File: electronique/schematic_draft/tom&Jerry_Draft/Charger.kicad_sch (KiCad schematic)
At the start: 20 parts, among them SW5 Switch, U1 MP1475DJ-LF-P

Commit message: STM32 KiCAD V2 - 18.09.2024
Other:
- note added: "3A"
- note removed: "Linear regulator"
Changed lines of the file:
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@@
+	)
+	(junction
+		(at 29.21 41.91)
+		(diameter 0)
+		(color 0 0 0 0)
 	)
 	(junction
@@
 	)
 	(junction
+		(at 58.42 74.93)
+		(diameter 0)
+		(color 0 0 0 0)
+	)
+	(junction
 		(at 44.45 54.61)
 		(diameter 0)
@@
 	)
 	(junction
+		(at 120.65 59.69)
+		(diameter 0)
+		(color 0 0 0 0)
+	)
+	(junction
 		(at 91.44 59.69)
 		(diameter 0)
@@
 	(wire
 		(pts
-			(xy 29.21 39.37) (xy 29.21 54.61)
+			(xy 29.21 39.37) (xy 29.21 41.91)
 		)
 		(stroke
@@
 		(pts
 			(xy 106.68 71.12) (xy 106.68 64.77)
+		)
+		(stroke
+			(width 0)
+			(type default)
+		)
+	)
+	(wire
+		(pts
+			(xy 29.21 41.91) (xy 29.21 54.61)
 		)
 		(stroke
@@
 		)
 	)
-	(text "Linear regulator\n\n\n"
-		(exclude_from_sim no)
-		(at 173.99 36.83 0)
-		(effects
-			(font
-				(size 4 4)
-				(bold yes)
-				(color 255 0 48 1)
-			)
-			(justify left bottom)
-		)
-	)
 	(text "recommanded components"
 		(exclude_from_sim no)
@@
 		)
 	)
-	(label "3A"
-		(at 114.3 59.69 0)
-		(fields_autoplaced yes)
+	(text "3A\n"
+		(exclude_from_sim no)
+		(at 116.332 59.182 0)
 		(effects
 			(font
 				(size 1.27 1.27)
 			)
-			(justify left bottom)
 		)
 	)
@@
 	)
 	(symbol
+		(lib_id "power:PWR_FLAG")
+		(at 29.21 41.91 90)
+		(unit 1)
+		(exclude_from_sim no)
+		(in_bom yes)
+		(on_board yes)
+		(dnp no)
+		(fields_autoplaced yes)
+		(property "Reference" "#FLG0201"
+			(at 27.305 41.91 0)
+			(effects
+				(font
+					(size 1.27 1.27)
+				)
+				(hide yes)
+			)
+		)
+		(property "Value" "PWR_FLAG"
+			(at 25.4 41.9099 90)
+			(effects
+				(font
+					(size 1.27 1.27)
+				)
+				(justify left)
+			)
+		)
+		(property "Footprint" ""
+			(at 29.21 41.91 0)
+			(effects
+				(font
+					(size 1.27 1.27)
+				)
+				(hide yes)
+			)
+		)
+		(property "Datasheet" "~"
+			(at 29.21 41.91 0)
+			(effects
+				(font
+					(size 1.27 1.27)
+				)
+				(hide yes)
+			)
+		)
+		(property "Description" "Special symbol for telling ERC where power comes from"
+			(at 29.21 41.91 0)
+			(effects
+				(font
+					(size 1.27 1.27)
+				)
+				(hide yes)
+			)
+		)
+		(pin "1"
+		)
+		(instances
+			(project ""
+				(path "/d6e3fbeb-d028-494d-83bf-2e4a8b12578d/8ac3fdfa-c0da-499a-9332-dcbe4f0edf5d"
+					(reference "#FLG0201")
+					(unit 1)
+				)
+			)
+		)
+	)
+	(symbol
 		(lib_id "Device:R_Small")
 		(at 82.55 71.12 90)
@@
 	)
 	(symbol
+		(lib_id "power:PWR_FLAG")
+		(at 120.65 59.69 270)
+		(unit 1)
+		(exclude_from_sim no)
+		(in_bom yes)
+		(on_board yes)
+		(dnp no)
+		(fields_autoplaced yes)
+		(property "Reference" "#FLG0202"
+			(at 122.555 59.69 0)
+			(effects
+				(font
+					(size 1.27 1.27)
+				)
+				(hide yes)
+			)
+		)
+		(property "Value" "PWR_FLAG"
+			(at 124.46 59.6899 90)
+			(effects
+				(font
+					(size 1.27 1.27)
+				)
+				(justify left)
+			)
+		)
+		(property "Footprint" ""
+			(at 120.65 59.69 0)
+			(effects
+				(font
+					(size 1.27 1.27)
+				)
+				(hide yes)
+			)
+		)
+		(property "Datasheet" "~"
+			(at 120.65 59.69 0)
+			(effects
+				(font
+					(size 1.27 1.27)
+				)
+				(hide yes)
+			)
+		)
+		(property "Description" "Special symbol for telling ERC where power comes from"
+			(at 120.65 59.69 0)
+			(effects
+				(font
+					(size 1.27 1.27)
+				)
+				(hide yes)
+			)
+		)
+		(pin "1"
+		)
+		(instances
+			(project "tom&Jerry_Draft"
+				(path "/d6e3fbeb-d028-494d-83bf-2e4a8b12578d/8ac3fdfa-c0da-499a-9332-dcbe4f0edf5d"
+					(reference "#FLG0202")
+					(unit 1)
+				)
+			)
+		)
+	)
+	(symbol
 		(lib_id "power:GND")
 		(at 95.25 52.07 180)
@@
 					(unit 1)
 				)
+			)
+		)
+	)
+	(symbol
+		(lib_id "power:PWR_FLAG")
+		(at 58.42 74.93 90)
+		(unit 1)
+		(exclude_from_sim no)
+		(in_bom yes)
+		(on_board yes)
+		(dnp no)
+		(fields_autoplaced yes)
+		(property "Reference" "#FLG0203"
+			(at 56.515 74.93 0)
+			(effects
+				(font
+					(size 1.27 1.27)
+				)
+				(hide yes)
+			)
+		)
+		(property "Value" "PWR_FLAG"
+			(at 54.61 74.9299 90)
+			(effects
+				(font
+					(size 1.27 1.27)
+				)
+				(justify left)
+			)
+		)
+		(property "Footprint" ""
+			(at 58.42 74.93 0)
+			(effects
+				(font
+					(size 1.27 1.27)
+				)
+				(hide yes)
+			)
+		)
+		(property "Datasheet" "~"
+			(at 58.42 74.93 0)
+			(effects
+				(font
+					(size 1.27 1.27)
+				)
+				(hide yes)
+			)
+		)
+		(property "Description" "Special symbol for telling ERC where power comes from"
+			(at 58.42 74.93 0)
+			(effects
+				(font
+					(size 1.27 1.27)
+				)
+				(hide yes)
+			)
+		)
+		(pin "1"
+		)
+		(instances
+			(project "tom&Jerry_Draft"
+				(path "/d6e3fbeb-d028-494d-83bf-2e4a8b12578d/8ac3fdfa-c0da-499a-9332-dcbe4f0edf5d"
+					(reference "#FLG0203")
+					(unit 1)
+				)

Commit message: KiCAD V3 - 18.09.2024
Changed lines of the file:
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@@
+	(wire
+		(pts
+			(xy 175.26 87.63) (xy 175.26 90.17)
+		)
+		(stroke
+			(width 0)
+			(type default)
+		)
+	)
 	(wire
 		(pts
@@
 		)
 	)
+	(hierarchical_label "CC2"
+		(shape input)
+		(at 175.26 90.17 0)
+		(fields_autoplaced yes)
+		(effects
+			(font
+				(size 1.27 1.27)
+			)
+			(justify left)
+		)
+	)
+	(hierarchical_label "CC1"
+		(shape input)
+		(at 175.26 87.63 0)
+		(fields_autoplaced yes)
+		(effects
+			(font
+				(size 1.27 1.27)
+			)
+			(justify left)
+		)
+	)

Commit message: STM32 KiCAD V5 - 20.09.2024
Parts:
- removed Alim_batterie1, Alim_charger1: Conn_01x02, Connector_JST:JST_XH_S2B-XH-A-1_1x02_P2.50mm_Horizontal, symbol Connector_Generic:Conn_01x02
- removed C10, C11, C9: 0.1uF, Capacitor_SMD:C_0603_1608Metric_Pad1.08x0.95mm_HandSolder, symbol Device:C_Small
- removed C12: 15pF, Capacitor_SMD:C_0603_1608Metric_Pad1.08x0.95mm_HandSolder, symbol Device:C_Small
- removed C13, C14, C8: 22uF, Capacitor_SMD:C_0603_1608Metric_Pad1.08x0.95mm_HandSolder, symbol Device:C_Small
- removed D7: 1.5KExxA, Library:SODFL3718X108N, symbol Diode:1.5KExxA
- removed F1: Polyfuse, Fuse:Fuse_1206_3216Metric, symbol Device:Polyfuse
- removed L2: 4.7uH, Library:INDPM4141X210N, symbol Device:L_Small
- removed R10: 20, Resistor_SMD:R_0805_2012Metric_Pad1.20x1.40mm_HandSolder, symbol Device:R_Small
- removed R11: 16k, Resistor_SMD:R_0603_1608Metric_Pad0.98x0.95mm_HandSolder, symbol Device:R_Small
- removed R12: 7.36k, Resistor_SMD:R_0603_1608Metric_Pad0.98x0.95mm_HandSolder, symbol Device:R_Small
- removed R13: 40.2k, Resistor_SMD:R_0603_1608Metric_Pad0.98x0.95mm_HandSolder, symbol Device:R_Small
- removed R8, R9: 100k, Resistor_SMD:R_0603_1608Metric_Pad0.98x0.95mm_HandSolder, symbol Device:R_Small
- removed SW5: Switch, Library:Switch-3, symbol Switch:SW_SPDT
- removed U1: MP1475DJ-LF-P, Library:SOT65P280X100-8N, symbol Ludzlib:MP1475
- added C201, C206, C207: 22uF, Capacitor_SMD:C_0603_1608Metric_Pad1.08x0.95mm_HandSolder, symbol Device:C_Small
- added C202, C203, C204: 0.1uF, Capacitor_SMD:C_0603_1608Metric_Pad1.08x0.95mm_HandSolder, symbol Device:C_Small
- added C205: 15pF, Capacitor_SMD:C_0603_1608Metric_Pad1.08x0.95mm_HandSolder, symbol Device:C_Small
- added C208, C209: 1uF, symbol Device:C
- added C210, C212: 10nF, symbol Device:C
- added C211: 100nF, symbol Device:C
- added C213: 1mF, symbol Device:C
- added D201: LED, symbol Device:LED
- added D202, D203: D, symbol Device:D
- added J201: USB_C_Receptacle_USB2.0_16P, symbol Connector:USB_C_Receptacle_USB2.0_16P
- added J202, J203: Conn_01x02, symbol Connector_Generic:Conn_01x02
- added JP201, JP202, JP203, JP204: SolderJumper_2_Open, symbol Jumper:SolderJumper_2_Open
- added L201: 4.7uH, Library:INDPM4141X210N, symbol Device:L_Small
- added PS201: BU33SD5WG-TR, BU33SD5WG-TR:SOT95P280X125-5N, symbol BU33SD5WG-TR:BU33SD5WG-TR
- added R201, R202: 100k, Resistor_SMD:R_0603_1608Metric_Pad0.98x0.95mm_HandSolder, symbol Device:R_Small
- added R203: 20, Resistor_SMD:R_0805_2012Metric_Pad1.20x1.40mm_HandSolder, symbol Device:R_Small
- added R204: 16k, Resistor_SMD:R_0603_1608Metric_Pad0.98x0.95mm_HandSolder, symbol Device:R_Small
- added R205: 7.36k, Resistor_SMD:R_0603_1608Metric_Pad0.98x0.95mm_HandSolder, symbol Device:R_Small
- added R206: 40.2k, Resistor_SMD:R_0603_1608Metric_Pad0.98x0.95mm_HandSolder, symbol Device:R_Small
- added R207: 3.6k, symbol Device:R
- added R208, R209: 27K, symbol Device:R
- added R210: 10k, symbol Device:R
- added R211: 15k, symbol Device:R
- added R212: 100m, symbol Device:R
- added U201: MP1475DJ-LF-P, Library:SOT65P280X100-8N, symbol Ludzlib:MP1475
- added U202: BQ25172DSGR, BQ25172DSGR:IC_BQ25172DSGR, symbol BQ25172:BQ25172DSGR
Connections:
- net +5V: now also C205.2, C206.1, C207.1, C208.1, L201.2, PS201.1 (VIN), PS201.3 (STBY), R206.2
- net +BATT: now also C201.1, C203.1, C211.1, C212.1, D202.1 (K), JP202.2 (B), R202.2, R212.1, U201.2 (IN)
- net CC1: now also J201.A5 (CC1)
- net GND: now also C201.2, C202.1, C203.2, C206.2, C207.2, C208.2, C209.2, C210.2, C211.2, C212.2, C213.2, J201.A1 (GND), J201.A12 (GND), J201.B1 (GND), J201.B12 (GND), J201.S1 (SHIELD), J202.1 (Pin_1), J203.1 (Pin_1), PS201.2 (GND), R205.1, R207.2, R208.2, R209.2, R210.2, R211.2, U201.4 (GND), U202.4 (GND), U202.9 (EXP)
- new net: C213.1, R212.2
- new net: C204.1, L201.1, U201.3 (SW)
- new net: C205.1, R204.2, R205.2, R206.1
- new net: R208.1, U202.6 (TMR)
- new net: JP204.1 (A), U202.1 (IN)
- new net: R209.1, U202.2 (ISET)
- new net: R210.1, U202.3 (TS)
- new net: D201.1 (K), U202.5 (STAT)
- new net: R207.1, U202.7 (VSET)
- new net: C210.1, D203.1 (K), R211.1
- new net: R201.1, U201.1 (PG)
- new net: C202.2, R201.2, U201.7 (VCC)
- new net: R204.1, U201.8 (FB)
- new net: R203.1, U201.5 (BST)
- new net: C204.2, R203.2
- new net: D202.2 (A), D203.2 (A), JP201.2 (B)
- new net: R202.1, U201.6 (EN/SYNC)
- new net +3.3V: C209.1, D201.2 (A), PS201.5 (VOUT)
- new net Batt_CHG: J201.A4 (VBUS), J201.A9 (VBUS), J201.B4 (VBUS), J201.B9 (VBUS), J202.2 (Pin_2), JP201.1 (A), JP204.2 (B)
- new net Batt_cell: J203.2 (Pin_2), JP203.1 (A), U202.8 (OUT)
- new net CC2: J201.B5 (CC2)
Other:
- note added: "Linear regulator"
- note added: "Valeure minimale des condo (cf doc)"
- note removed: "3A"
- note removed: "Accepted current 1.5A Max current 3A ->5s"
- note removed: "Enable alway one"
- note removed: "recommanded components"

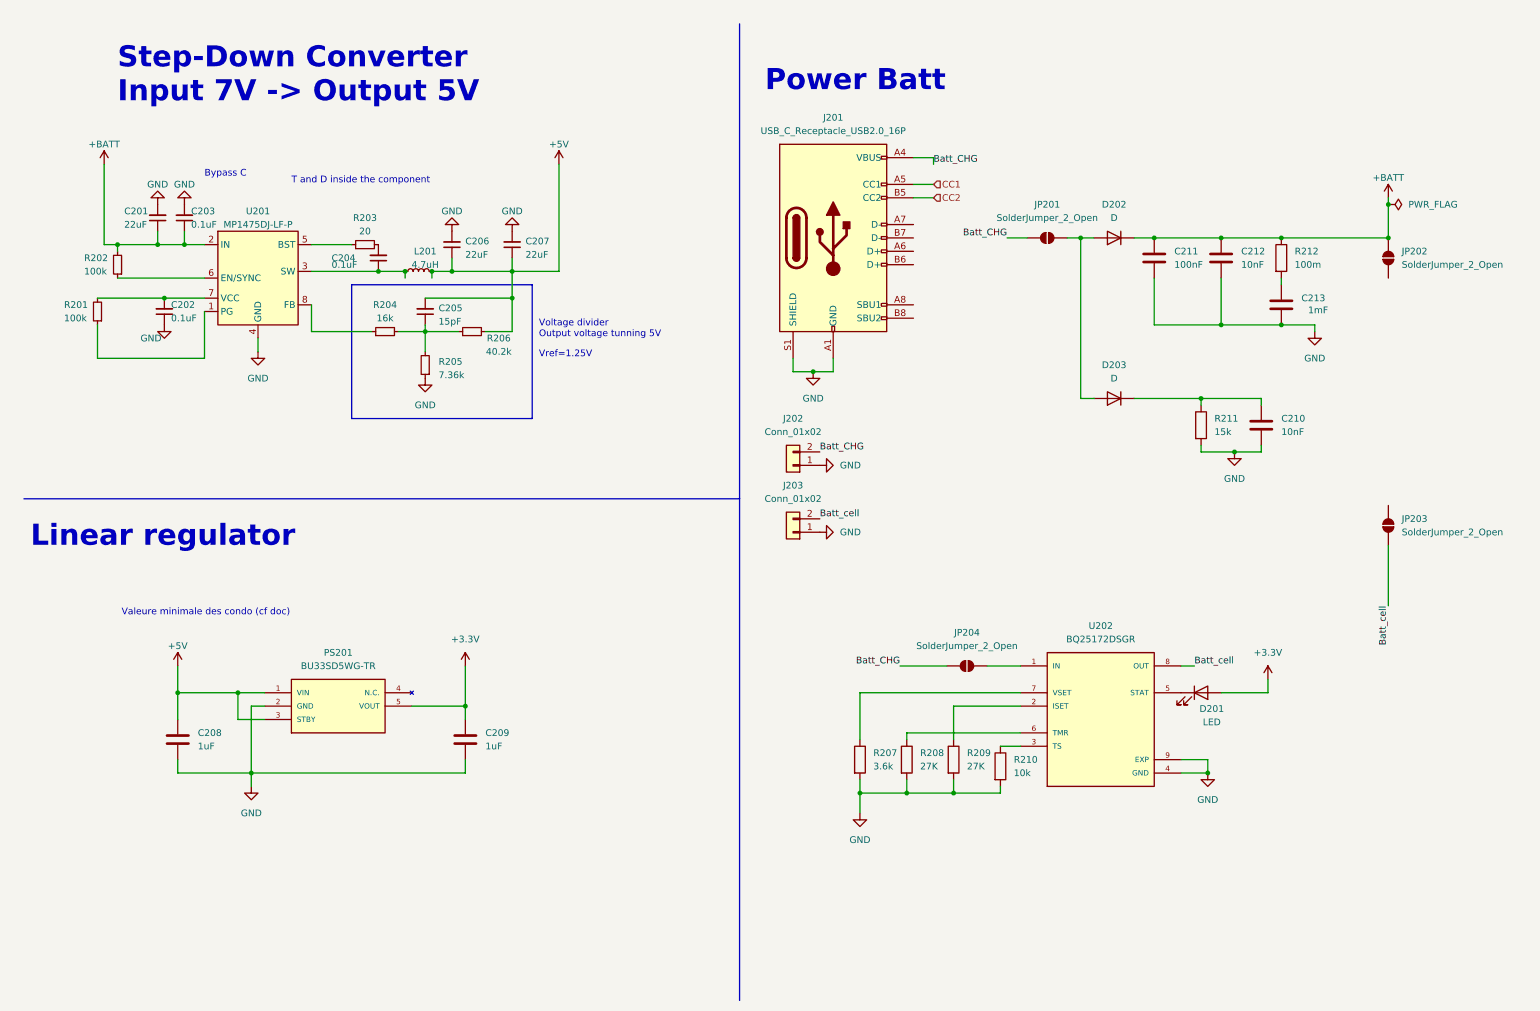
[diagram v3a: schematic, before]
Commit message: STM32 KiCAD V5 - 25.09.2024 - Ajout connecteurs TOF, ...
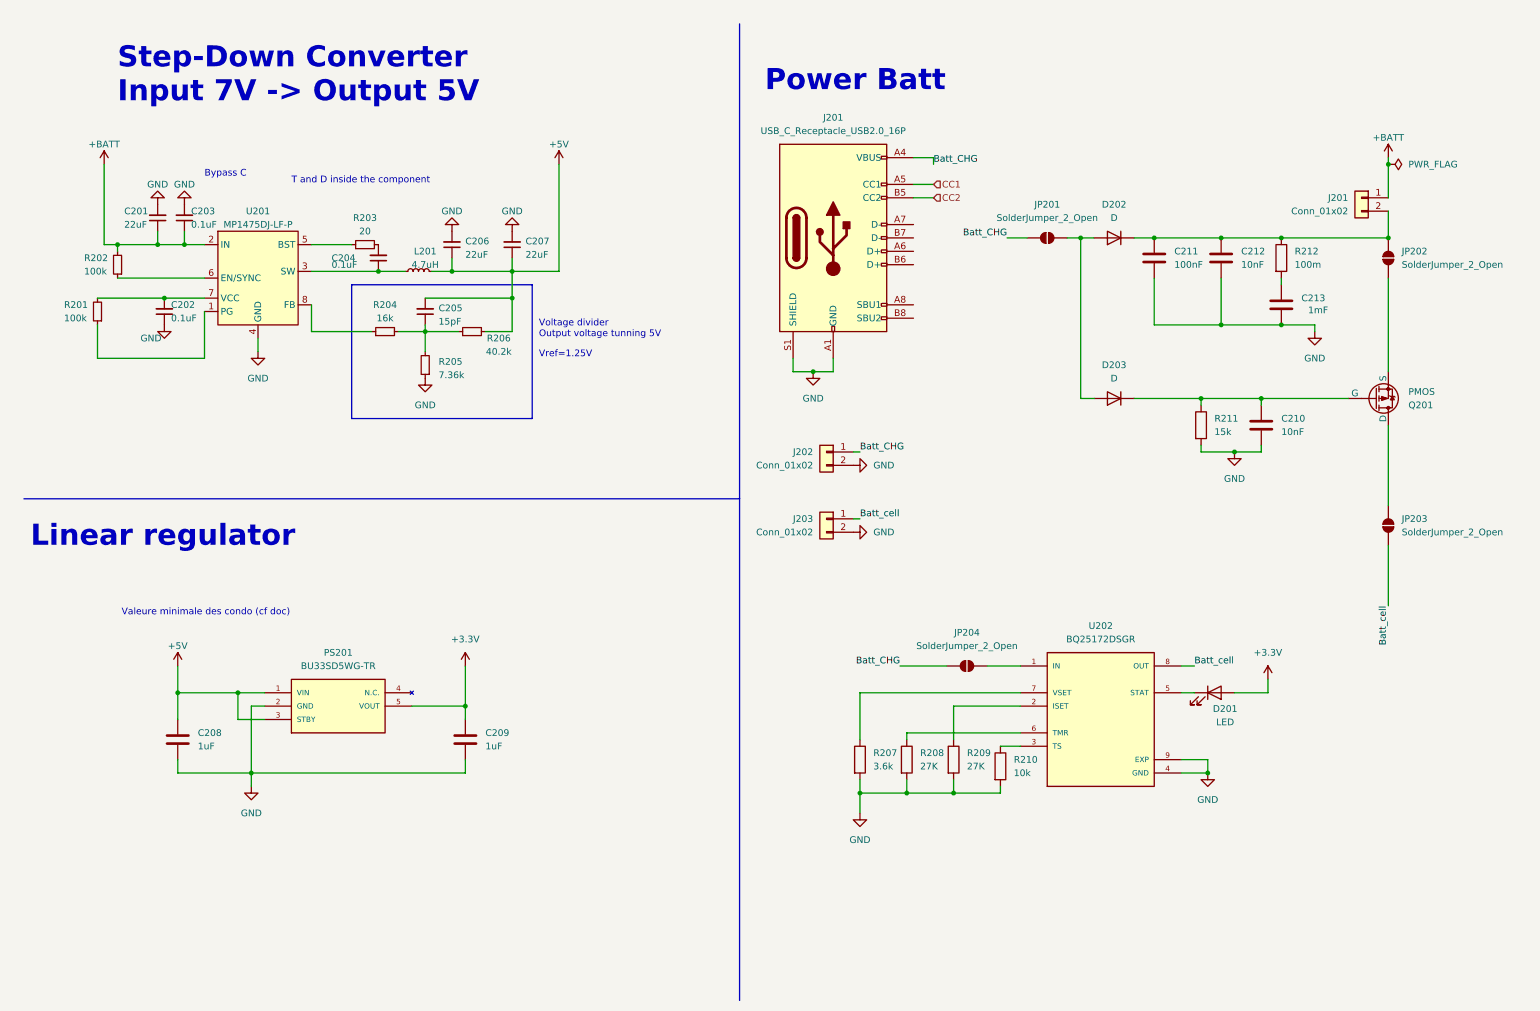
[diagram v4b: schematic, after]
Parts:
- added J201: Conn_01x02, symbol Connector_Generic:Conn_01x02
- added Q201: PMOS, symbol Simulation_SPICE:PMOS
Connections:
- net +BATT: now also J201.1 (Pin_1); no longer C211.1, C212.1, D202.1 (K), JP202.2 (B), R212.1
- net Batt_CHG: now also J202.1 (Pin_1); no longer J202.2 (Pin_2)
- net Batt_cell: now also J203.1 (Pin_1); no longer J203.2 (Pin_2)
- net GND: now also J202.2 (Pin_2), J203.2 (Pin_2); no longer J202.1 (Pin_1), J203.1 (Pin_1)
- net at C210.1, D203.1 (K), R211.1: now also Q201.2 (G)
- net at JP202.1 (A): now also Q201.3 (S)
- net at JP203.2 (B): now also Q201.1 (D)
- new net: C211.1, C212.1, D202.1 (K), J201.2 (Pin_2), JP202.2 (B), R212.1
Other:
- moved on the sheet: D201, J202, J203

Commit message: STM32 KiCAD V6 - 25.09.2024 - Ajout des points test
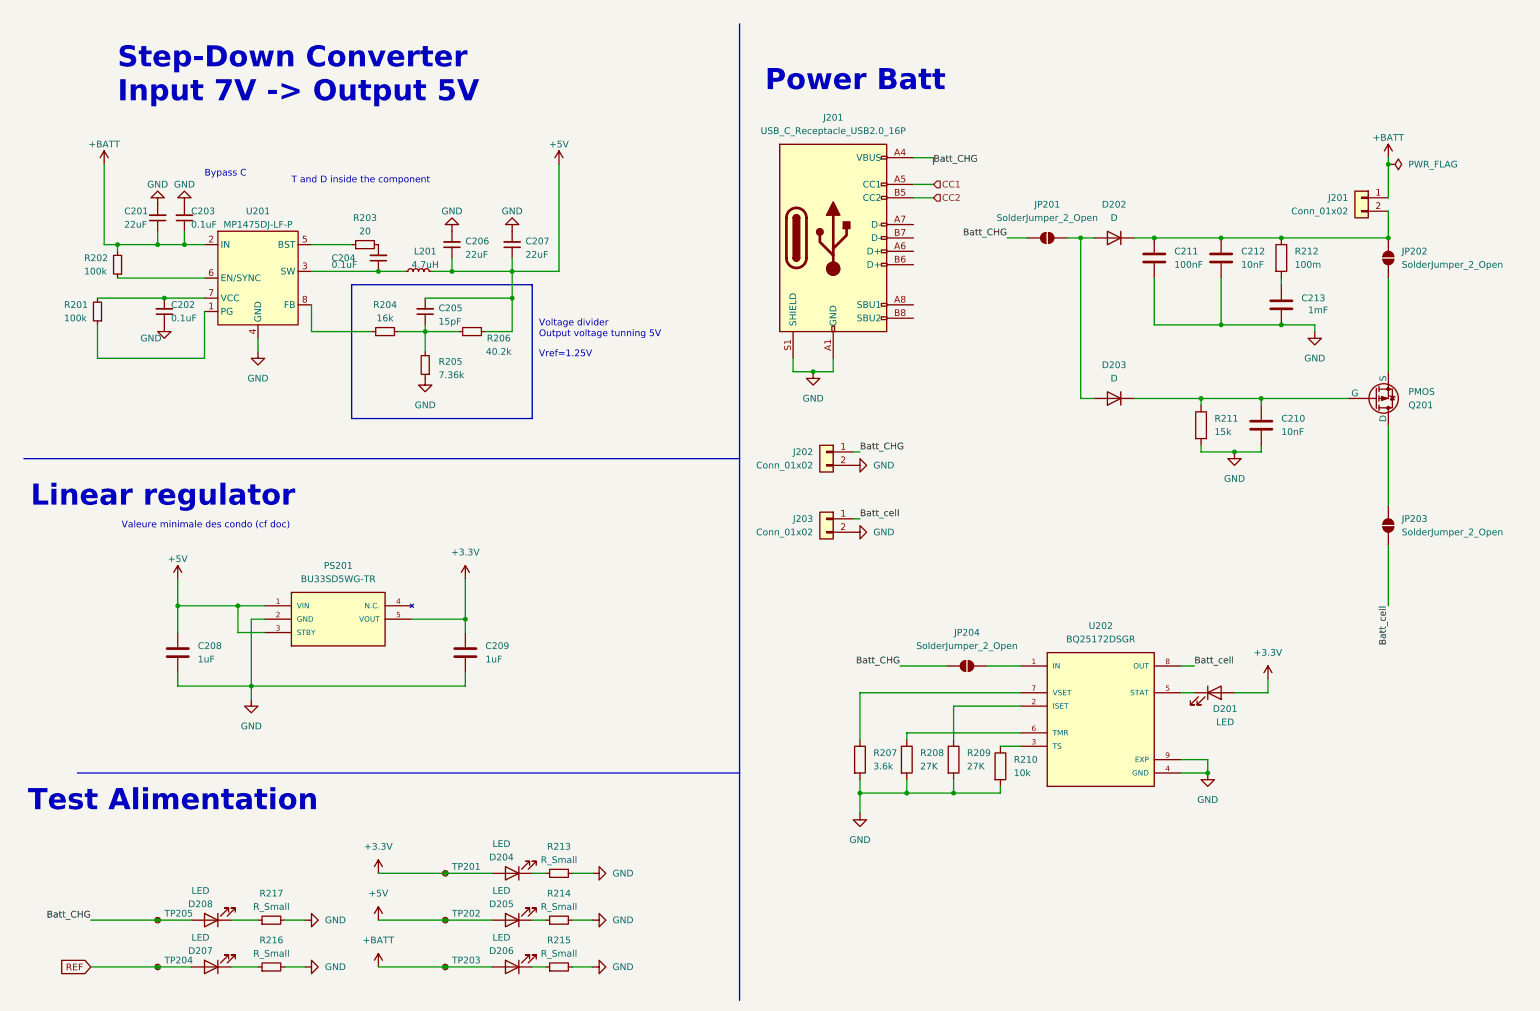
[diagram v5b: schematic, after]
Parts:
- added D204, D205, D206, D207, D208: LED, symbol Device:LED
- added R213, R214, R215, R216, R217: R_Small, symbol Device:R_Small
- added TP201, TP202, TP203, TP204, TP205: TestPoint_Small, symbol Connector:TestPoint_Small
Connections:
- net +3.3V: now also D204.2 (A), TP201.1
- net +5V: now also D205.2 (A), TP202.1
- net +BATT: now also D206.2 (A), TP203.1
- net Batt_CHG: now also D208.2 (A), TP205.1
- net GND: now also R213.2, R214.2, R215.2, R216.2, R217.2
- new net: D206.1 (K), R215.1
- new net: D204.1 (K), R213.1
- new net: D207.1 (K), R216.1
- new net: D208.1 (K), R217.1
- new net: D205.1 (K), R214.1
- new net REF: D207.2 (A), TP204.1
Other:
- note added: "Test Alimentation"
- moved on the sheet: C208, C209, PS201
